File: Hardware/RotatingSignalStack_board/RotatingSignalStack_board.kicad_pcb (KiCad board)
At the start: 2 copper layers, 69.1 x 69 mm, 32 parts, among them J1 8P8C_LED_Shielded, J2 Conn_01x05_Pin, SW1 SW_Push, SW2 SW_Push, U1 OKI, U3 Teensy4.1_DEV-16771

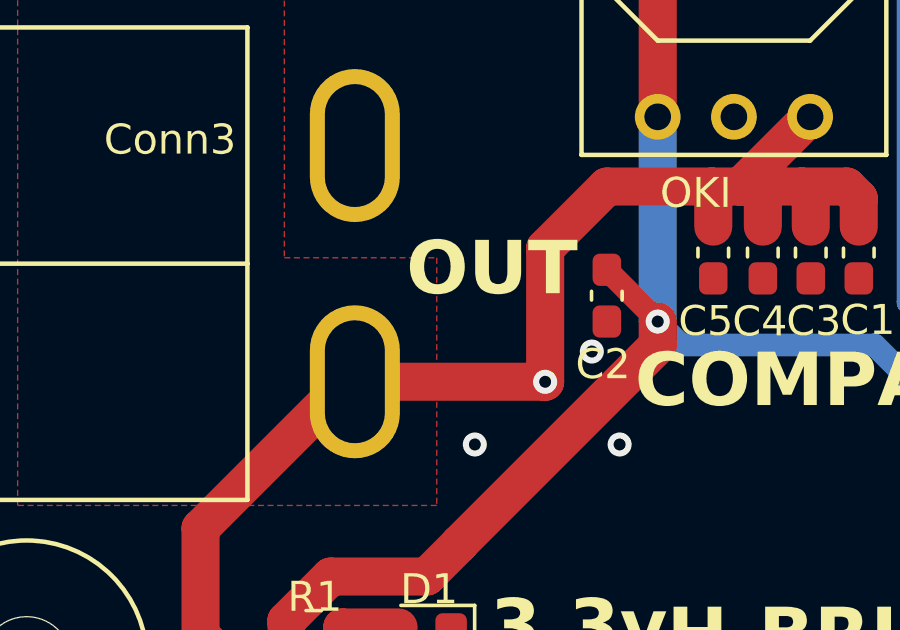
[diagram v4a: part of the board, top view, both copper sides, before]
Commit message: removed weird 12vOUT via, removed 90degree trace
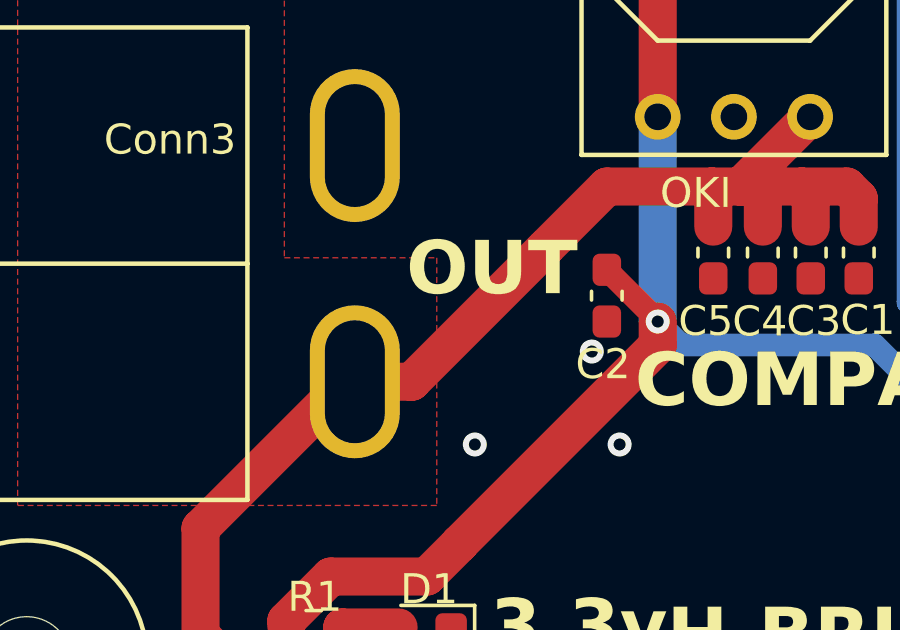
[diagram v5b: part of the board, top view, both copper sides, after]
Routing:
- net +12V: track 45.1 -> 42.5 mm, vias 1 -> 0
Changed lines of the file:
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@@
   (segment (start 122.428 147.828) (end 122.428 144.272) (width 1.27) (layer "F.Cu") (net 1))
   (segment (start 142.472 132.88) (end 140.972 132.88) (width 1.27) (layer "F.Cu") (net 1))
-  (segment (start 127.5722 139.388) (end 133.916 139.388) (width 1.27) (layer "F.Cu") (net 1))
+  (segment (start 127.5722 139.388) (end 129.464 139.388) (width 1.27) (layer "F.Cu") (net 1))
   (segment (start 135.972 132.88) (end 139.472 132.88) (width 1.27) (layer "F.Cu") (net 1))
   (segment (start 142.76975 134.2175) (end 142.76975 133.17775) (width 1.27) (layer "F.Cu") (net 1))
@@
   (segment (start 142.76975 133.17775) (end 142.472 132.88) (width 1.27) (layer "F.Cu") (net 1))
   (segment (start 141.172 133.08) (end 140.972 132.88) (width 1.27) (layer "F.Cu") (net 1))
+  (segment (start 129.464 139.388) (end 133.916 134.936) (width 1.27) (layer "F.Cu") (net 1))
   (segment (start 127.312 139.388) (end 127.5722 139.388) (width 1.27) (layer "F.Cu") (net 1))
   (segment (start 125.288 149.82) (end 124.42 149.82) (width 1.27) (layer "F.Cu") (net 1))
   (segment (start 139.51975 134.2175) (end 139.51975 132.92775) (width 1.27) (layer "F.Cu") (net 1))
-  (segment (start 133.916 139.388) (end 133.916 134.936) (width 1.27) (layer "F.Cu") (net 1))
   (segment (start 133.916 134.936) (end 135.972 132.88) (width 1.27) (layer "F.Cu") (net 1))
   (segment (start 139.51975 132.92775) (end 139.472 132.88) (width 1.27) (layer "F.Cu") (net 1))
@@
   (segment (start 144.36975 134.2175) (end 144.36975 133.27775) (width 1.27) (layer "F.Cu") (net 1))
   (segment (start 124.42 149.82) (end 122.428 147.828) (width 1.27) (layer "F.Cu") (net 1))
-  (via (at 133.916 139.388) (size 0.8) (drill 0.4) (layers "F.Cu" "B.Cu") (net 1))
   (via (at 131.572 141.478) (size 0.8) (drill 0.4) (layers "F.Cu" "B.Cu") (free) (net 2))
   (via (at 151.972 129.38) (size 0.8) (drill 0.4) (layers "F.Cu" "B.Cu") (free) (net 2))

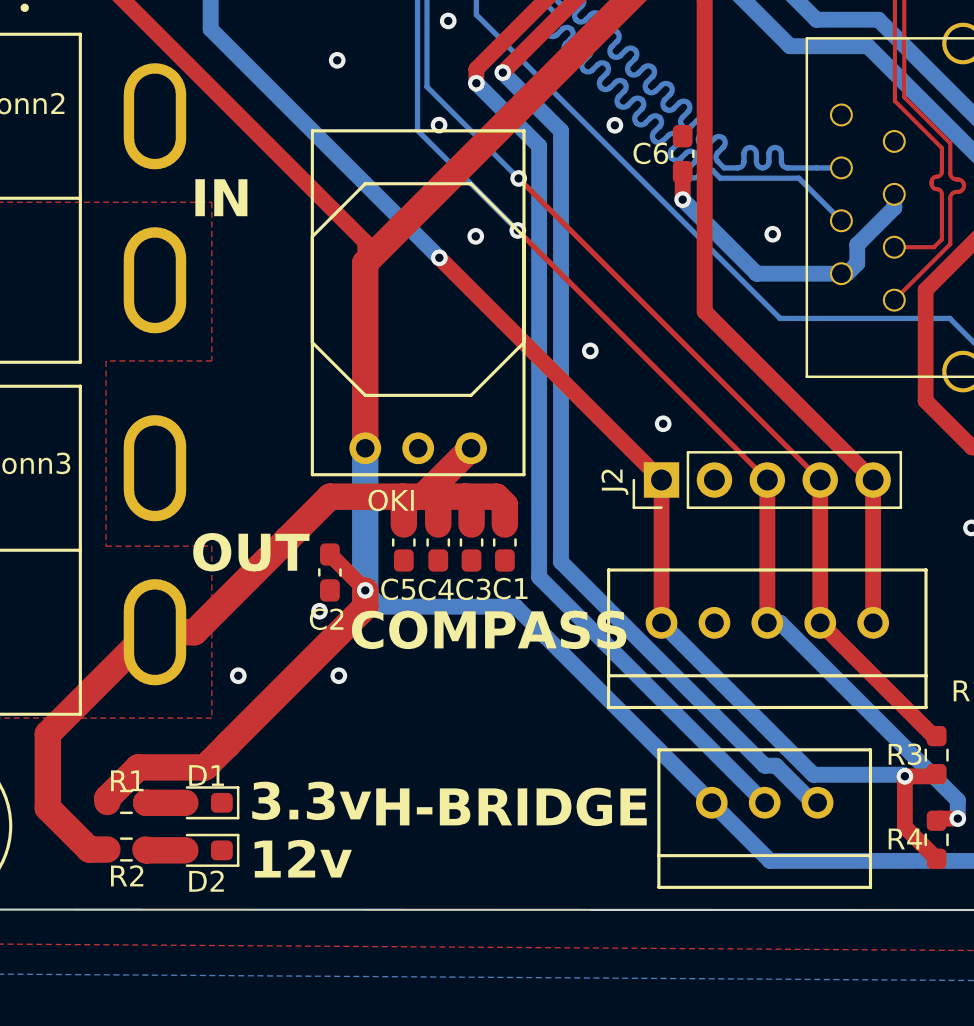
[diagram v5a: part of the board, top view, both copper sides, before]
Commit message: trace cleanup, moved ethernet cap closer to J1
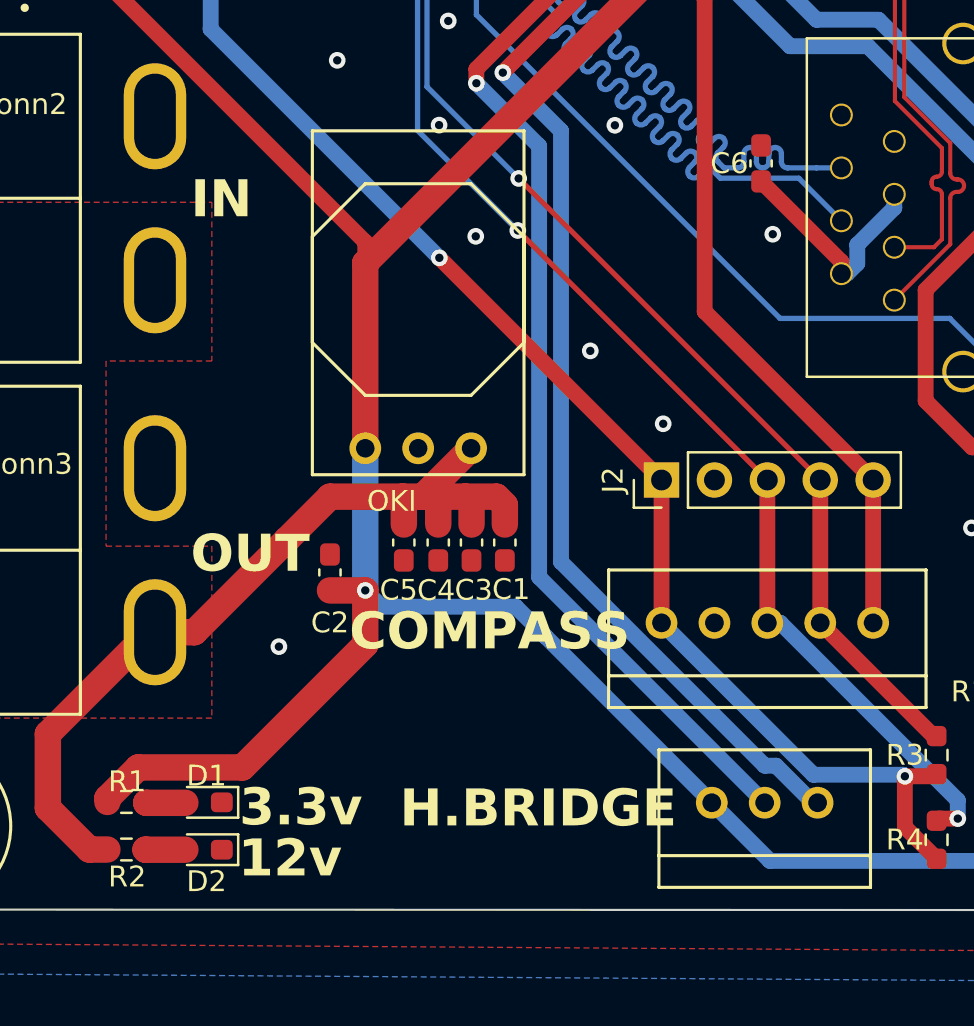
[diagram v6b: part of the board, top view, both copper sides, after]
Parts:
- moved C6 3.79 mm to (156.7, 116.9)
- turned C2 to 90 degrees
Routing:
- net Net-(C6-Pad1): track 15.4 -> 11.0 mm, vias 1 -> 0
- net GND: vias 16 -> 14
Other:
- board text added: "H.BRIDGE"
- board text removed: "H-BRIDGE"
